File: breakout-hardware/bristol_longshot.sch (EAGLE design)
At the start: 66 parts, among them U3 74LVC1G04GW

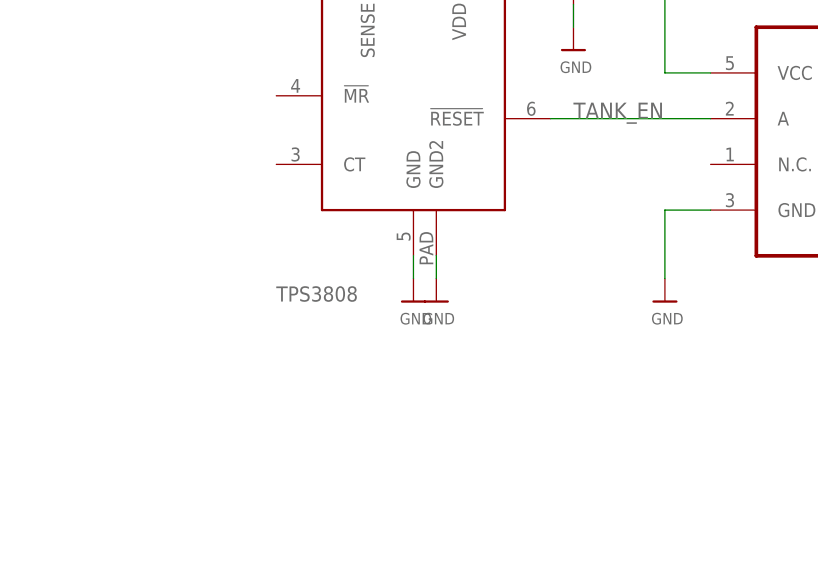
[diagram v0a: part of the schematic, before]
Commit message: Added note about Ct on supervisor
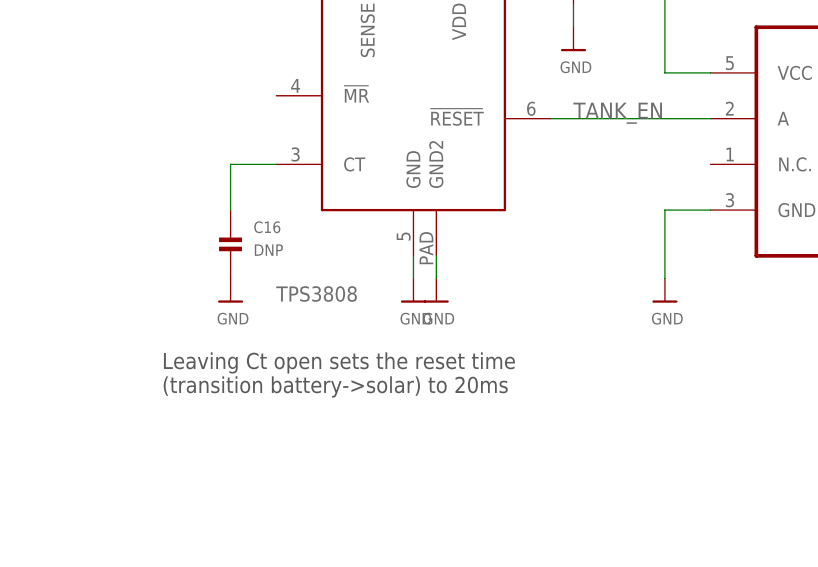
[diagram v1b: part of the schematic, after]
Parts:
- added C16: DNP, microbuilder_v3:CAP_CERAMIC_0402
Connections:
- new net N$2: C16.P$1, U$63.CT
- net GND: now also C16.P$2
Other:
- note added: "Leaving Ct open sets the reset time (transition battery->solar) to 20ms"
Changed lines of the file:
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@@
 <part name="C15" library="resistor" deviceset="C-EU" device="C0603K" value="10µF"/>
 <part name="U$37" library="microbuilder_v3" deviceset="GND" device=""/>
+<part name="C16" library="microbuilder_v3" deviceset="CAP_CERAMIC" device="_0402" value="DNP"/>
+<part name="U$52" library="microbuilder_v3" deviceset="GND" device=""/>
 </parts>
 <sheets>
@@
 <text x="426.72" y="73.66" size="1.778" layer="97">End of charge current = 52.5 / Rend
 10kΩ ==&gt; 5mA</text>
+<text x="510.54" y="68.58" size="1.778" layer="97">Leaving Ct open sets the reset time
+(transition battery-&gt;solar) to 20ms</text>
 </plain>
 <instances>
@@
 <instance part="C15" gate="G$1" x="728.98" y="88.9"/>
 <instance part="U$37" gate="G$1" x="728.98" y="78.74"/>
+<instance part="C16" gate="G$1" x="518.16" y="83.82"/>
+<instance part="U$52" gate="G$1" x="518.16" y="78.74"/>
 </instances>
 <busses>
@@
 <pinref part="U$37" gate="G$1" pin="GND"/>
 <wire x1="728.98" y1="83.82" x2="728.98" y2="81.28" width="0.1524" layer="91"/>
+</segment>
+<segment>
+<pinref part="C16" gate="G$1" pin="P$2"/>
+<pinref part="U$52" gate="G$1" pin="GND"/>
 </segment>
 </net>
@@
 </segment>
 </net>
+<net name="N$2" class="0">
+<segment>
+<pinref part="U$63" gate="G$1" pin="CT"/>
+<pinref part="C16" gate="G$1" pin="P$1"/>
+<wire x1="523.24" y1="93.98" x2="518.16" y2="93.98" width="0.1524" layer="91"/>
+<wire x1="518.16" y1="93.98" x2="518.16" y2="88.9" width="0.1524" layer="91"/>
+</segment>
+</net>

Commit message: Added pdf of breakout
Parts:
- removed C20: 1nF, microbuilder_v3:CAP_CERAMIC_0402
- removed U$51: L6924D, l6924d:L6924D
- added C17: 10µF, resistor:C-EUC0603K
- added U7: 74LVC1G04GW, 74LVC1G04GW_inverter:74LVC1G04GW
- C1, C3, C4: value 1nF -> 4.7µF
- C10: value 47nF -> 1nF
- C13: value 4.7µF -> 47nF
- C14: value 1nF -> DNP
- C15: value 10µF -> 4.7µF; device resistor:C-EUC0603K -> microbuilder_v3:CAP_CERAMIC_0402
- C16: value DNP -> 4.7µF
- C5, C6, C7, C8: value 4.7µF -> 1nF
- R1, R3: value 820kΩ -> 1kΩ
- R10: value 1kΩ -> 100kΩ
- R11: value 1kΩ -> 47kΩ
- R12: value 100kΩ -> 47kΩ
- R13, R14: value 1kΩ -> 10kΩ
- R2, R4: value 2M2Ω -> 1kΩ
- R5: value 47kΩ -> 2M2Ω
- R6: value 100kΩ -> 2M2Ω
- R7: value 47kΩ -> 820kΩ
- R8: value 10kΩ -> 820kΩ
- R9: value 10kΩ -> 100kΩ
- U3: value 74LVC1G04GW -> L6924D; device 74LVC1G04GW_inverter:74LVC1G04GW -> l6924d:L6924D
- renumbered C22 to C18, L8 to L4, U$1 to U1, U$38 to U2, U$61 to U5, U$62 to U4, U$63 to U6, U$64 to D3, U$65 to D4
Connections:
- net 1.8V: now also C17.1, L3.2; no longer C15.1, L1.2
- net BATTERY: now also C16.P$1, U3.VOSNS, U3.VOUT; no longer C8.P$1, U$51.VOSNS, U$51.VOUT
- net BATTERY_EN: now also R14.1, U7.Y; no longer R9.1, U3.Y
- net GND: now also C15.P$2, C17.2, C3.P$2, C4.P$2, C5.P$1, C6.P$1, R11.2, R13.1, R9.1, U3.GND2, U3.VOPRG, U7.GND; no longer C15.2, C20.P$2, C3.P$1, C4.P$1, C5.P$2, C6.P$2, R1.1, R3.1, R5.2, U$51.GND, U$51.GND2, U$51.VOPRG
- net IPRE: now also U3.IPRE; no longer U$51.IPRE
- net LX1: now also L1.2; no longer L2.2
- net LX2: now also L2.2; no longer L3.2
- net MPP-SET2: now also C6.P$2, R2.2; no longer C3.P$2, R10.2
- net MPPT-VOUT-1: now also R5.2; no longer R2.2
- net MPPT-VOUT-2: now also R6.2; no longer R4.2
- net N$1: now also C5.P$2, R1.2; no longer C4.P$2, R11.2
- net N$2: now also C14.P$1; no longer C16.P$1
- net N$3: now also C13.P$1, U3.TPRG; no longer C10.P$1, U$51.TPRG
- net N$6: now also R3.1; no longer R13.1
- net N$8: now also R4.1; no longer R14.1
- net PV1: now also C1.P$1, L1.1, R1.1; no longer C5.P$1, L2.1, R11.1
- net PV2: now also C3.P$1, C4.P$1, L2.1, R2.1; no longer C6.P$1, C7.P$1, L3.1, R10.1
- net REND: now also R13.2, U3.IEND; no longer R8.2, U$51.IEND
- net RPRG: now also R12.2, U3.IPRG; no longer R7.2, U$51.IPRG
- net SD: now also R9.2, U3.SD; no longer R12.2, U$51.SD
- net SPV_VCTRL1: now also C7.P$1, R5.1, R7.2; no longer C1.P$1, R1.2, R2.1
- net SPV_VCTRL2: now also C8.P$1, R6.1, R8.2; no longer C20.P$1, R3.2, R4.1
- net ST1: now also U3.ST1; no longer U$51.ST1
- net ST2: now also U3.ST2; no longer U$51.ST2
- net SUPERVISOR_VCC: now also C10.P$1, R14.2, U7.VCC; no longer C14.P$1, R9.2, U3.VCC
- net TANK: now also C15.P$1, R3.2, R4.2, U3.VIN, U3.VINSNS; no longer C13.P$1, R13.2, R14.2, U$51.VIN, U$51.VINSNS
- net TANK_BUCK_SW: now also L3.1; no longer L1.1
- net TANK_EN: now also U7.A; no longer U3.A
- net TH: now also R10.2, R11.1, U3.TH; no longer R5.1, R6.2, U$51.TH
- net VPRE: now also U3.VPRE; no longer U$51.VPRE
- net VREF: now also R10.1, U3.VREF; no longer R6.1, U$51.VREF
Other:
- moved on the sheet: C1, C10, C12, C13, C14, C15, C16, C2, C3, C4, C5, C6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

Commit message: Second revision. Modifications:
-Ref des inductors for mppt
-Pull-up on tank en
-Li-ion charger to LT4054
-Add TVS diods for mppt
-Capacitors both sides of jumpers
-More current in Vctrl divider. TODO partslist for this
-Fixed cream on supervisor
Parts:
- removed C9: 1nF, microbuilder_v3:CAP_CERAMIC_0402
- removed D1: GREEN, led:LEDCHIPLED_0603
- removed L1, L2: 2.2µH, SparkFun:INDUCTOR1007
- removed R11, R12: 47kΩ, microbuilder_v3:RESISTOR_0402
- removed R13, R14: 10kΩ, microbuilder_v3:RESISTOR_0402
- added C19: 10µF, resistor:C-EUC0603K
- added D5, D6: DIODE[TVS], nxp:DIODE[TVS]
- added U$25: S1751-46R, Harwin-Test-Point:S1751-46R
- added U$5, U$6: XAL6060, XAL6060:XAL6060
- C13: value 47nF -> 4.7µF
- C14: value DNP -> 4.7µF
- R10: value 100kΩ -> 330Ω
- R3, R4: value 1kΩ -> 10kΩ
- R5, R6: value 2M2Ω -> 220kΩ
- R7, R8: value 820kΩ -> 82kΩ
- R9: value 100kΩ -> 2.2kΩ
- U3: value L6924D -> LT4054ES5-4.2; device l6924d:L6924D -> XYKlib:LT4054ES5-4.2
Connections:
- removed net IPRE: U3.IPRE
- removed net N$2: C14.P$1, U6.CT
- removed net N$3: C13.P$1, U3.TPRG
- removed net N$6: D1.A, R3.1
- removed net N$8: D2.A, R4.1
- removed net REND: R13.2, U3.IEND
- removed net RPRG: R12.2, U3.IPRG
- removed net SD: JP6.2, R9.2, U3.SD
- removed net ST1: D1.C, U3.ST1
- removed net ST2: D2.C, U3.ST2
- removed net TH: R10.2, R11.1, U3.TH
- removed net VPRE: U3.VPRE
- removed net VREF: C9.P$2, R10.1, U3.VREF
- new net CHG: D2.C, U3.CHRG
- new net CHG_LED: D2.A, R10.1
- new net CT: U6.CT
- new net N$5: JP6.1, R9.1
- new net PROG: R9.2, U$25.1, U3.PROG
- net 1.8V: now also C19.1
- net BATTERY: now also U3.BAT; no longer U3.VOSNS, U3.VOUT
- net BATTERY_EN: now also R3.1; no longer R14.1
- net GND: now also C19.2, D5.1, D6.1, JP6.2; no longer C9.P$1, R11.2, R12.1, R13.1, R9.1, U3.GND2, U3.VOPRG
- net LX1: now also U$5.2; no longer L1.2
- net LX2: now also U$6.2; no longer L2.2
- net MPPT-VOUT-1: now also C13.P$1, D5.2
- net MPPT-VOUT-2: now also C14.P$1, D6.2
- net PV1: now also U$5.1; no longer L1.1
- net PV2: now also U$6.1; no longer L2.1
- net SUPERVISOR_VCC: now also R3.2, R4.2; no longer R14.2
- net TANK: now also R10.2, U3.VCC; no longer JP6.1, R3.2, R4.2, U3.VIN, U3.VINSNS
- net TANK_EN: now also R4.1
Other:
- note added: "!MR! has internal pull-up"
- note added: "Choose so total current through divider is 2µA - 20µA"
- note added: "Ichg = 150V / Rchg"
- note added: "Ichg can be measured by Vprog"
- note added: "Rchg = 2.2kΩ gives Ichg = 70mA"
- note added: "Recommended input cap is 1µF"
- note added: "Vout = 1.25(R1/R2 + 1)"
- note removed: "Charge Current = 11685 / Rprg 47kΩ ==> 250mA"
- note removed: "Ctprg sets the maximum charging time to 24h, and maximum precharge time to 3h for Rprg = 47kΩ"
- note removed: "End of charge current = 52.5 / Rend 10kΩ ==> 5mA"
- note removed: "Ipre is floating, giving a default pre-charge current of 10% = 25mA"
- note removed: "TH is unused, so is set at 0.6V for charge always enabled."
- note removed: "This is an upper limit that should never be reached, putting us in quasi-pulse mode instead."
- note removed: "Voprg = GND, so Vout = 4.2V"
- note removed: "Vpre is floating, giving a default pre-charge threshold of 2.8V"
- moved on the sheet: C11, C13, C14, C15, C16, C17, C18, D2, JP1, JP6, L3, L4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
